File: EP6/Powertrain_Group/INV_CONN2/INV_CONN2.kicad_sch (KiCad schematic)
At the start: 9 parts, among them J1 encoder, J12 Encoder, J13 motorTemp, J2 encoder, J3 PWR, J4 SIN, J5 COS

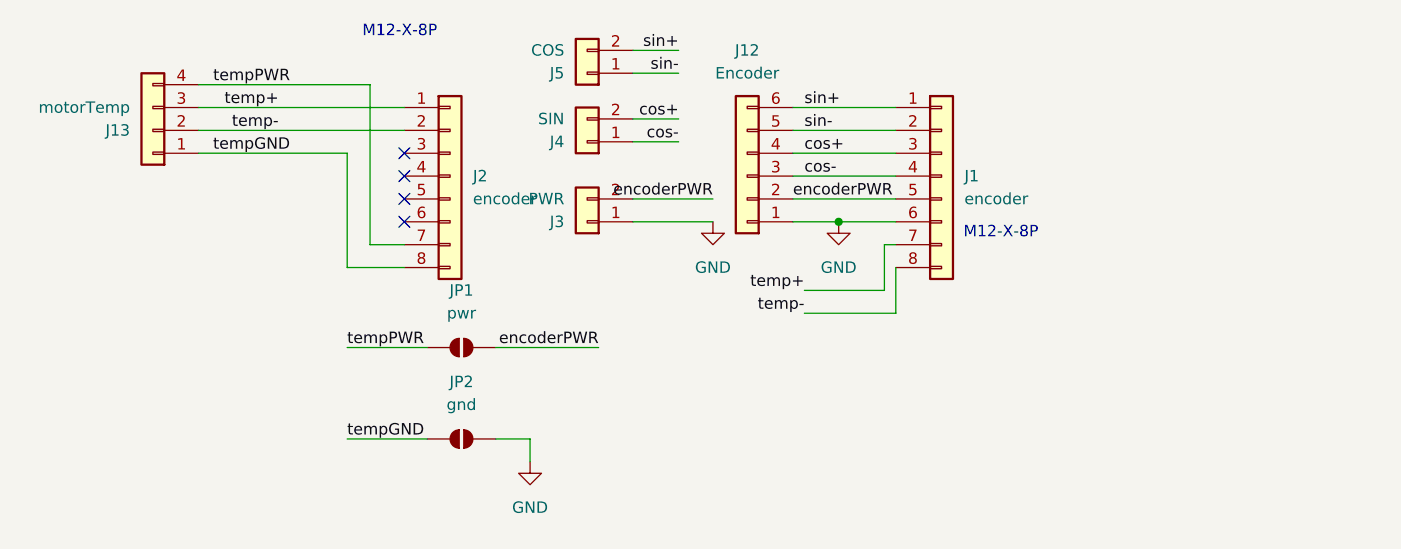
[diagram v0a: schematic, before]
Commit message: update INV_CONN2 to V1.1
change temp pinout to match encoder pinout
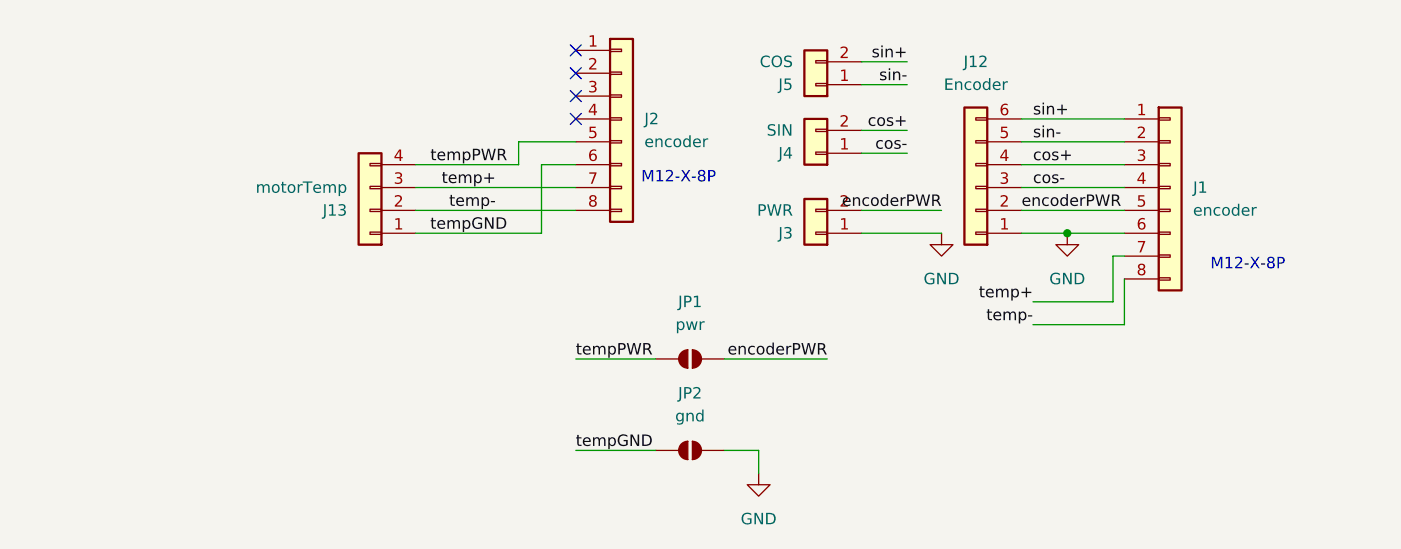
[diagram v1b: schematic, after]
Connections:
- net temp+: now also J2.7 (Pin_7); no longer J2.1 (Pin_1)
- net temp-: now also J2.8 (Pin_8); no longer J2.2 (Pin_2)
- net tempGND: now also J2.6 (Pin_6); no longer J2.8 (Pin_8)
- net tempPWR: now also J2.5 (Pin_5); no longer J2.7 (Pin_7)
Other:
- moved on the sheet: J1, J12, J13, J2, J3, J4, J5, JP1, JP2

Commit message: update INV_CONN2 to V1.2
V1.2 switch to JST 2.0 mm
     remove encoder individual 3p conns
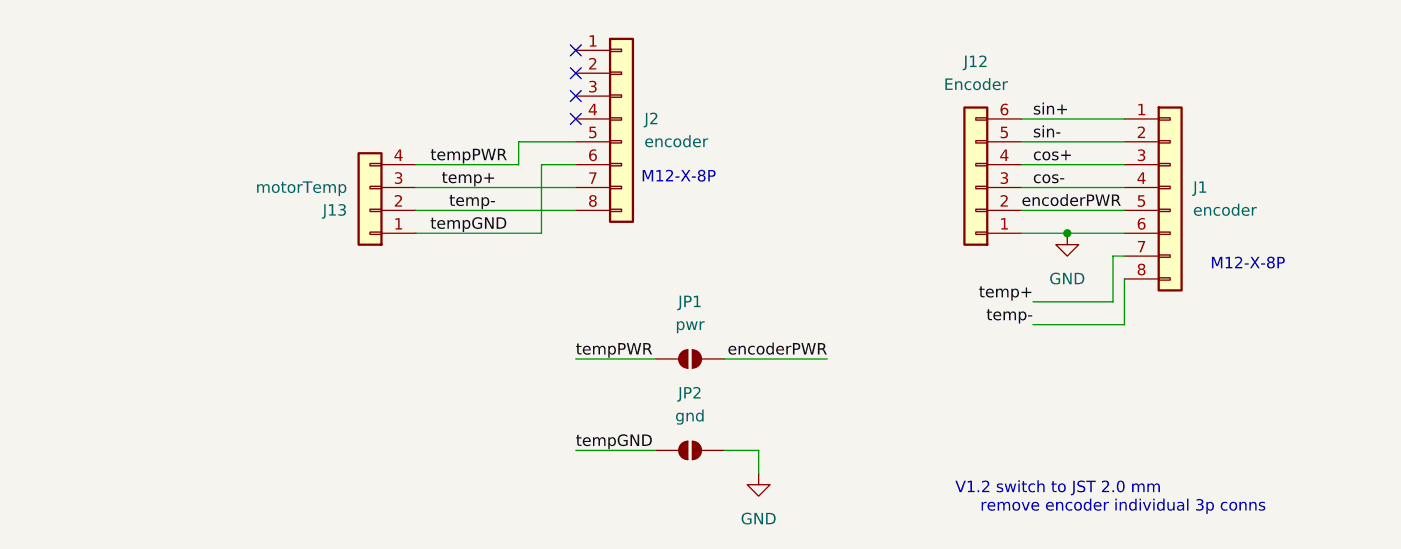
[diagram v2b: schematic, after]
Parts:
- removed J3: PWR, Connector_JST:JST_XH_B2B-XH-A_1x02_P2.50mm_Vertical, symbol Connector_Generic:Conn_01x02
- removed J4: SIN, Connector_JST:JST_XH_B2B-XH-A_1x02_P2.50mm_Vertical, symbol Connector_Generic:Conn_01x02
- removed J5: COS, Connector_JST:JST_XH_B2B-XH-A_1x02_P2.50mm_Vertical, symbol Connector_Generic:Conn_01x02
- J12: footprint Connector_JST:JST_XH_B6B-XH-A_1x06_P2.50mm_Vertical -> Connector_JST:JST_PH_B6B-PH-K_1x06_P2.00mm_Vertical
- J13: footprint Connector_JST:JST_XH_B4B-XH-A_1x04_P2.50mm_Vertical -> Connector_JST:JST_PH_B4B-PH-K_1x04_P2.00mm_Vertical
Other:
- note added: "V1.2 switch to JST 2.0 mm remove encoder individual 3p conns"
